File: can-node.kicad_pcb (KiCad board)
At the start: 2 copper layers, 68.6 x 66.8 mm, 36 parts, among them J1 Conn_01x02_Pin, J10 Conn_01x06_Pin, J11 Conn_01x02_Socket, J13 SDA, J14 SCL, J15 Conn_01x03_Pin, J17 Conn_01x02_Pin, J2 Conn_01x02_Pin, J3 RJ45, J4 RJ45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

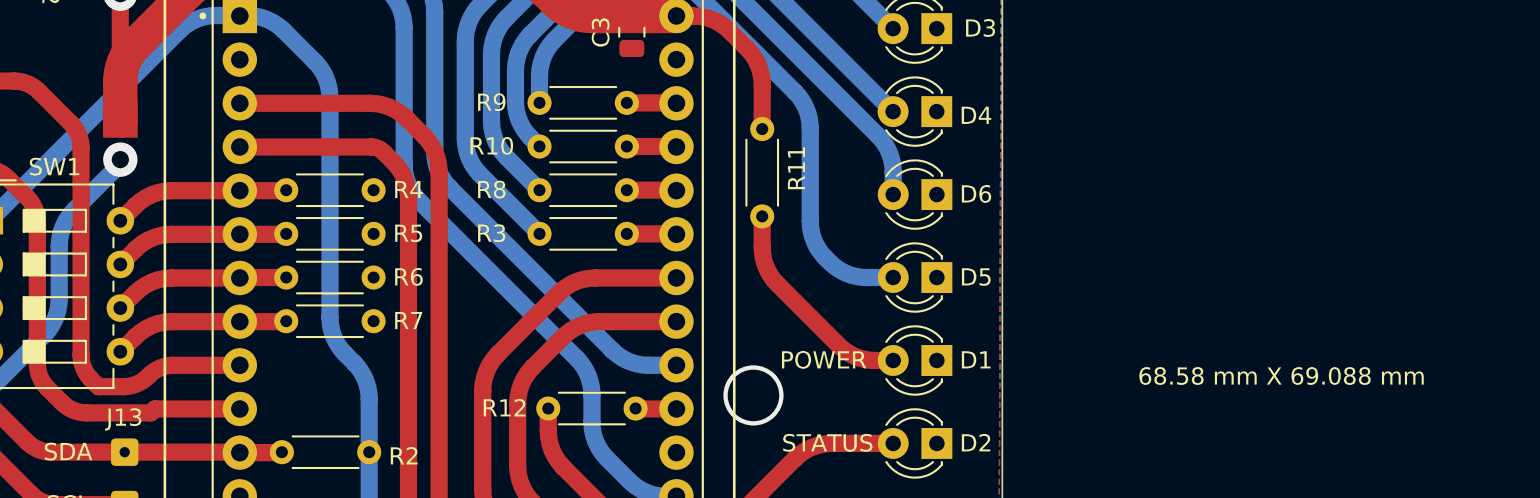
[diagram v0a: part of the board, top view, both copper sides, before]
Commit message: debug 5V trace
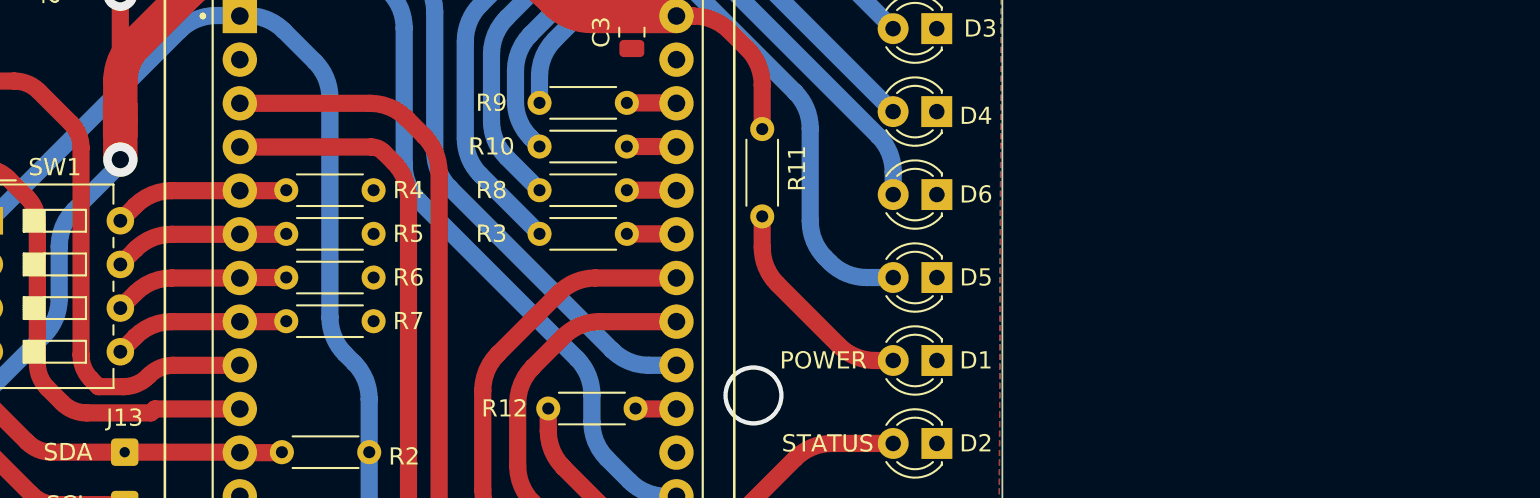
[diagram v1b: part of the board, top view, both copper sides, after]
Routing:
- net +5V: track 95.4 -> 97.7 mm
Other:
- board text removed: "68.58 mm X 69.088 mm"
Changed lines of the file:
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@@
   (gr_rect (start 102.921368 44.590812) (end 136.042369 105.651812)
     (stroke (width 0.15) (type default)) (fill none) (layer "F.CrtYd"))
-  (gr_text "68.58 mm X 69.088 mm" (at 159.512 80.772) (layer "F.SilkS")
-    (effects (font (size 1 1) (thickness 0.15)) (justify left bottom))
-  )
   (via (at 133.340815 103.061312) (size 3.5) (drill 3) (layers "F.Cu" "B.Cu") (net 0))
   (via (at 140.462 49.276) (size 3.5) (drill 3) (layers "F.Cu" "B.Cu") (net 0))
@@
   (segment (start 100.33 63.001641) (end 100.33 65.278) (width 2) (layer "F.Cu") (net 1))
   (segment (start 137.668 63.218641) (end 137.668 65.786) (width 1) (layer "F.Cu") (net 1))
+  (segment (start 100.33 67.564) (end 100.33 65.278) (width 2) (layer "F.Cu") (net 1))
   (segment (start 132.681 59.208) (end 133.657359 59.208) (width 1) (layer "F.Cu") (net 1))
   (segment (start 125.08468 57.77468) (end 125.639321 58.329321) (width 2) (layer "F.Cu") (net 1))

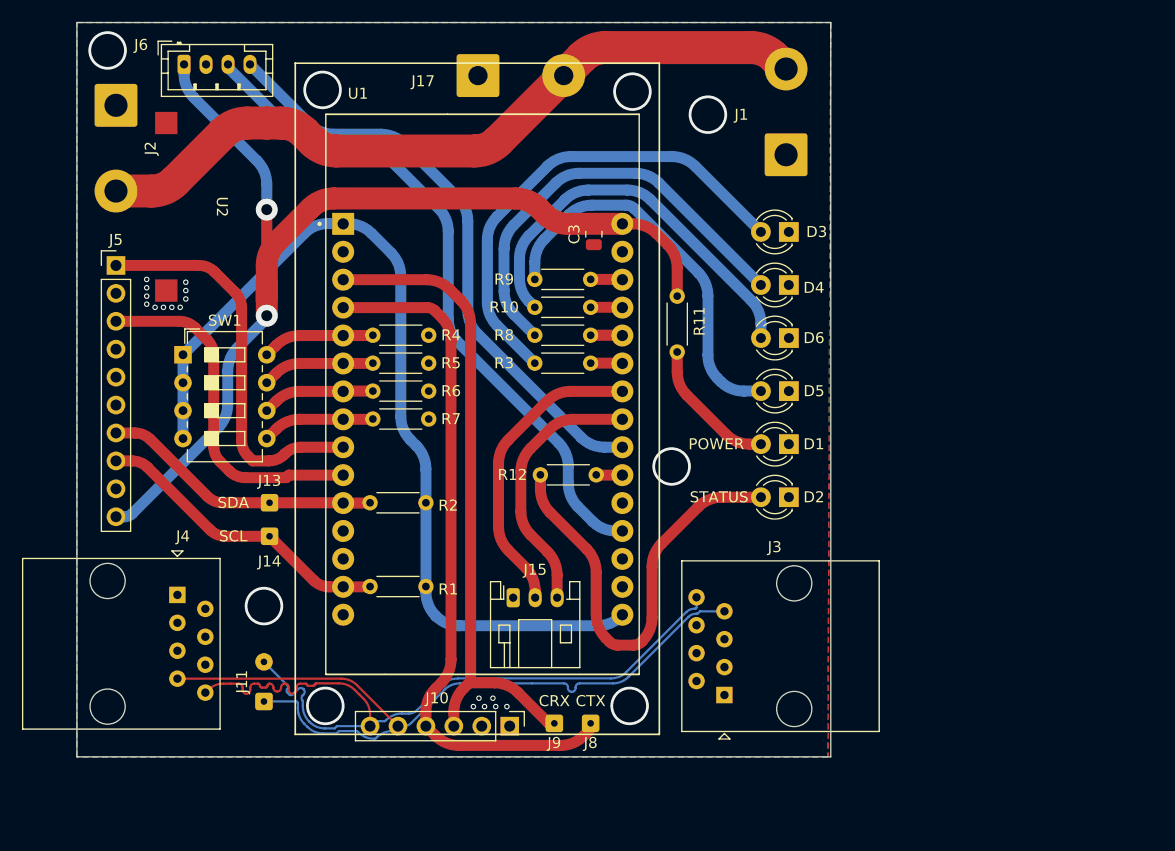
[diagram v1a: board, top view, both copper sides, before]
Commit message: add silkscreen
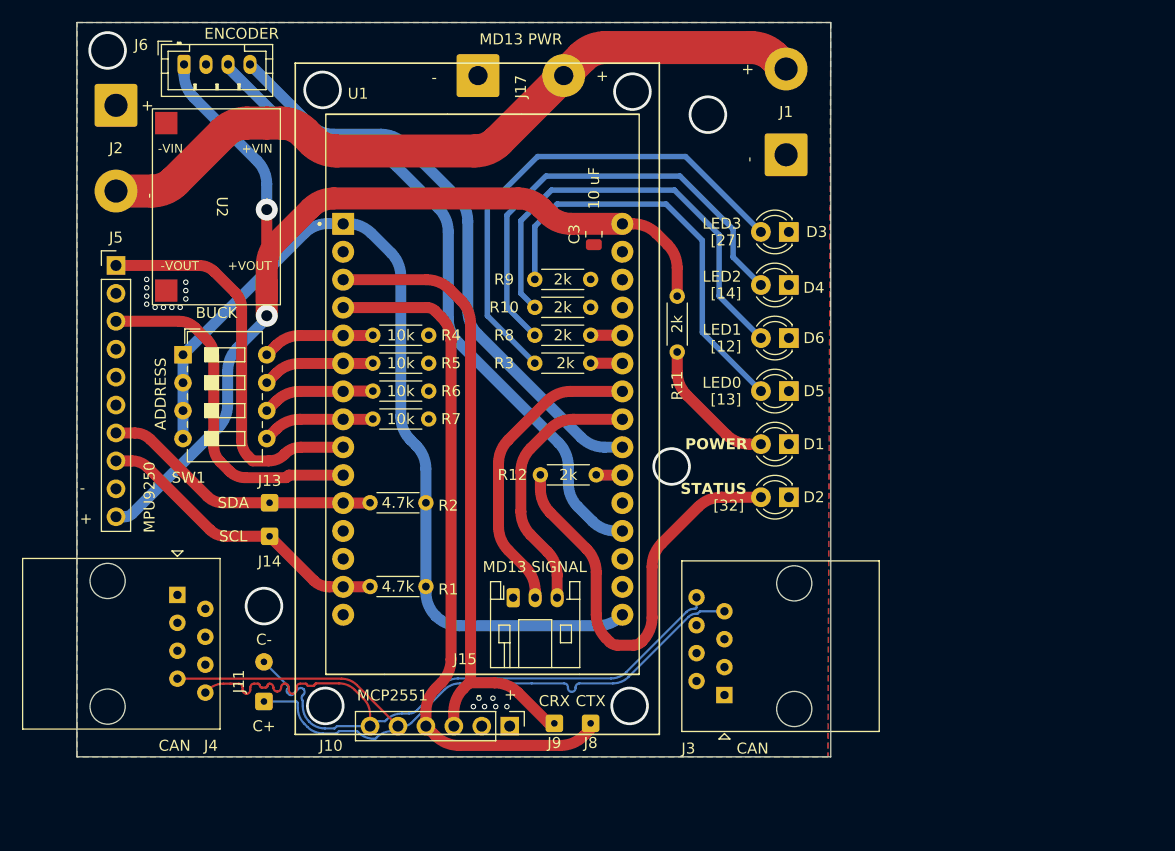
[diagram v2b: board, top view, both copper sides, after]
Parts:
- D3: value LED -> LED3
- D4: value LED -> LED2
- D5: value LED -> LED0
- D6: value LED -> LED1
- J10: value Conn_01x06_Pin -> MCP2551
- J15: value Conn_01x03_Pin -> MD13 SIGNAL
- J17: value Conn_01x02_Pin -> MD13 PWR
- J3, J4: value RJ45 -> CAN
- J5: value Conn_01x10_Pin -> MPU9250
- J6: value Conn_01x04_Pin -> ENCODER
- SW1: value SW_DIP_x04 -> ADDRESS
- U2: value ~ -> BUCK
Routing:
- net Net-(D6-A): track 36.6 -> 40.3 mm
- net LED1: track 2.90 -> 0.00 mm
- net LED0: track 2.90 -> 0.00 mm
- net Net-(D4-A): track 39.6 -> 42.2 mm
- net Net-(D5-A): track 35.9 -> 38.2 mm
- net Net-(D3-A): track 44.0 -> 45.6 mm
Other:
- board text added: "+"
- board text added: "+VIN"
- board text added: "+VOUT"
- board text added: "-"
- board text added: "-VIN"
- board text added: "-VOUT"
- board text added: "C+"
- board text added: "C-"
- board text added: "[12]"
- board text added: "[13]"
- board text added: "[14]"
- board text added: "[27]"
- board text added: "[32]"

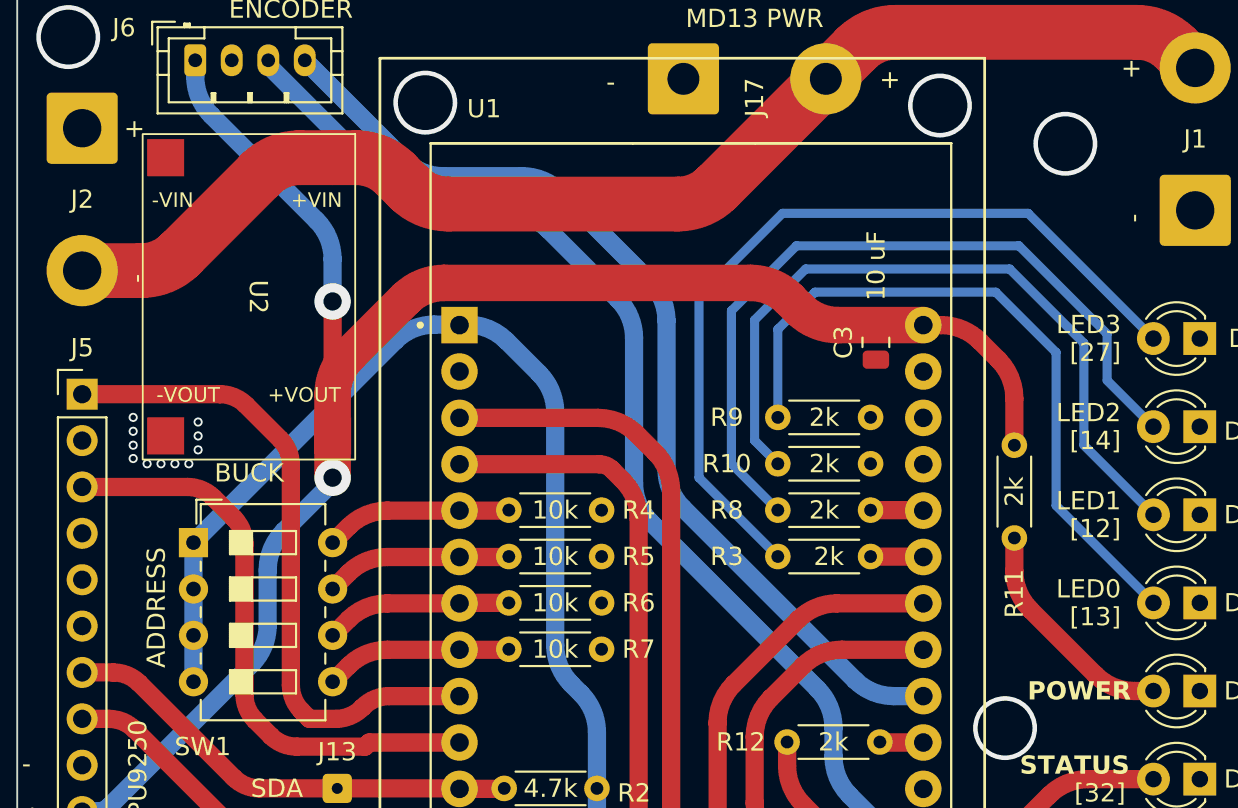
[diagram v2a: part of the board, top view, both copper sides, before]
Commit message: add CAN Rx & CAN Tx LEDs
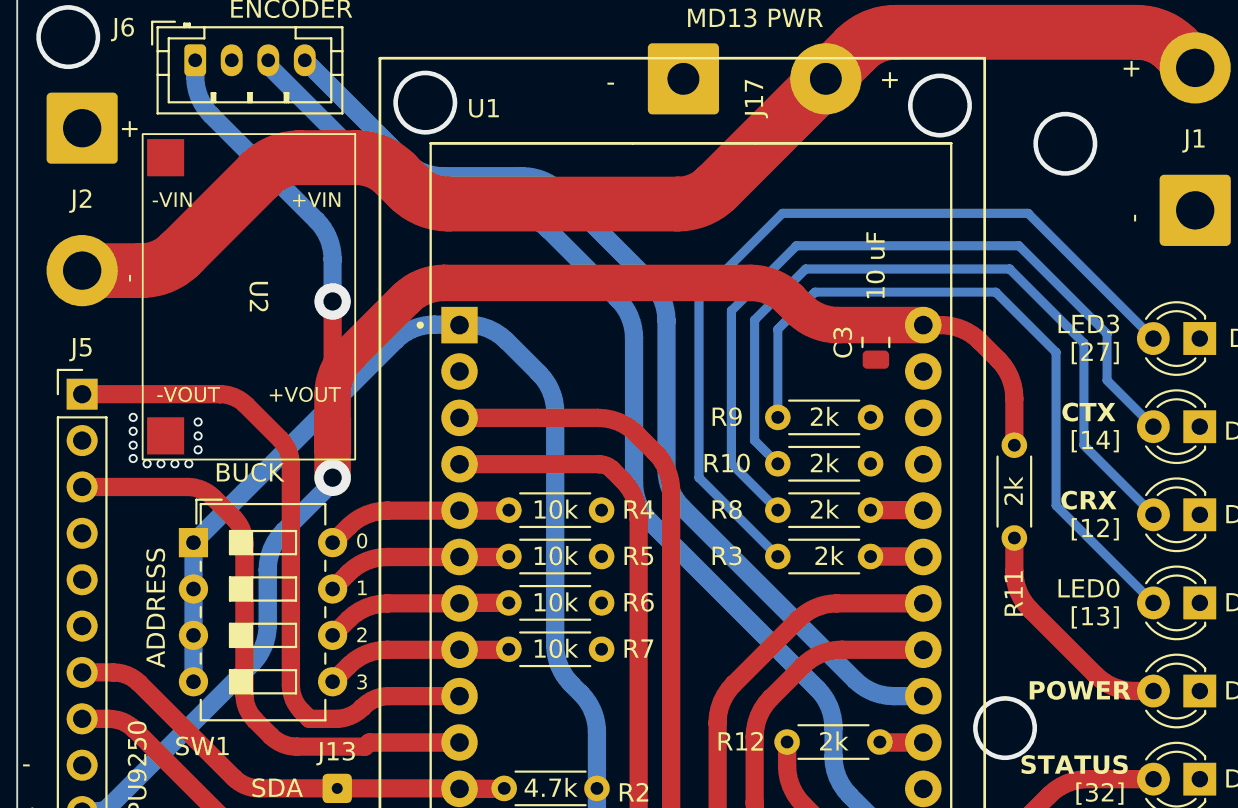
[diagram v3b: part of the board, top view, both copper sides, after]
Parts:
- D4: value LED2 -> CTX
- D6: value LED1 -> CRX
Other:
- board text added: "0 1 2 3"
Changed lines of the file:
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@@
         (effects (font (size 1 1) (thickness 0.15)))
     )
-    (fp_text value "LED1" (at 6.096 0.762) (layer "F.SilkS")
-        (effects (font (size 1 1) (thickness 0.15)))
+    (fp_text value "CRX" (at 6.096 0.762) (layer "F.SilkS" knockout)
+        (effects (font (size 1 1) (thickness 0.2) bold))
     )
     (fp_line (start -0.29 -1.236) (end -0.29 -1.08)
@@
       (rotate (xyz 0 0 0))
     )
+    (model "D:/anujv/Documents/KiCad/7.0/3dmodels/RJ45_SS_6488_FLS_Stewart.step"
+      (offset (xyz 4.5 -6.5 0))
+      (scale (xyz 1 1 1))
+      (rotate (xyz 0 0 0))
+    )
   )
   (footprint "Resistor_THT:R_Axial_DIN0204_L3.6mm_D1.6mm_P5.08mm_Horizontal" (layer "F.Cu")
@@
         (effects (font (size 1 1) (thickness 0.15)))
     )
-    (fp_text value "LED2" (at 6.091 0.762) (layer "F.SilkS")
-        (effects (font (size 1 1) (thickness 0.15)))
+    (fp_text value "CTX" (at 6.091 0.762) (layer "F.SilkS" knockout)
+        (effects (font (size 1 1) (thickness 0.2) bold))
     )
     (fp_line (start -0.29 -1.236) (end -0.29 -1.08)
@@
         (effects (font (size 1 1) (thickness 0.15)))
     )
-    (fp_text value "CAN" (at 13.716 0.254 -180) (layer "F.SilkS")
+    (fp_text value "CAN" (at 13.716 0.254) (layer "F.SilkS")
         (effects (font (size 1 1) (thickness 0.15)))
     )
@@
       (rotate (xyz 0 0 0))
     )
+    (model "D:/anujv/Documents/KiCad/7.0/3dmodels/RJ45_SS_6488_FLS_Stewart.step"
+      (offset (xyz 4.5 -6.5 0))
+      (scale (xyz 1 1 1))
+      (rotate (xyz 0 0 0))
+    )
   )
   (footprint "Connector_JST:JST_PH_S3B-PH-K_1x03_P2.00mm_Horizontal" (layer "F.Cu")
@@
     (effects (font (size 1 1) (thickness 0.15)) (justify left bottom))
   )
+  (gr_text "0\n\n1\n\n2\n\n3" (at 101.6 79.248) (layer "F.SilkS")
+    (effects (font (size 0.8 0.8) (thickness 0.15)) (justify left bottom))
+  )
   (gr_text "C-" (at 100.076 97.028) (layer "F.SilkS")
     (effects (font (size 1 1) (thickness 0.15)))
@@
     (effects (font (size 1 1) (thickness 0.15)) (justify left bottom))
   )
-  (gr_text "-" (at 90.17 56.896 90) (layer "F.SilkS")
+  (gr_text "-" (at 89.733741 56.884211 90) (layer "F.SilkS")
     (effects (font (size 1 1) (thickness 0.15)) (justify left bottom))
   )
@@
     (effects (font (size 1 1) (thickness 0.15)) (justify right))
   )
-  (gr_text "+" (at 88.9 49.022) (layer "F.SilkS")
+  (gr_text "+" (at 88.646 49.022) (layer "F.SilkS")
     (effects (font (size 1 1) (thickness 0.15)) (justify left bottom))
   )
@@
     (connect_pads yes (clearance 0.5))
     (min_thickness 1) (filled_areas_thickness no)
-    (fill (thermal_gap 1) (thermal_bridge_width 1) (smoothing fillet) (radius 3))
+    (fill yes (thermal_gap 1) (thermal_bridge_width 1) (smoothing fillet) (radius 3))
     (polygon
       (pts

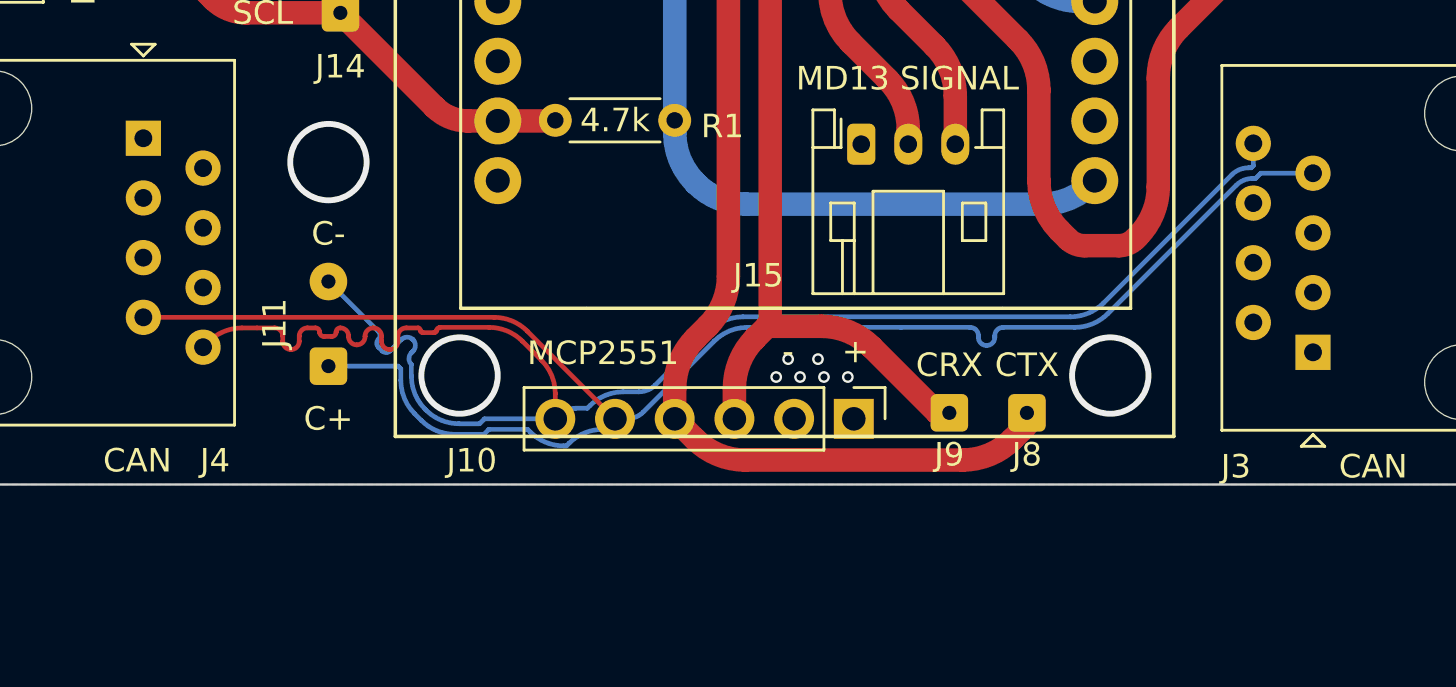
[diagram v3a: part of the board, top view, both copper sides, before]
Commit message: delete traces and move jumpers
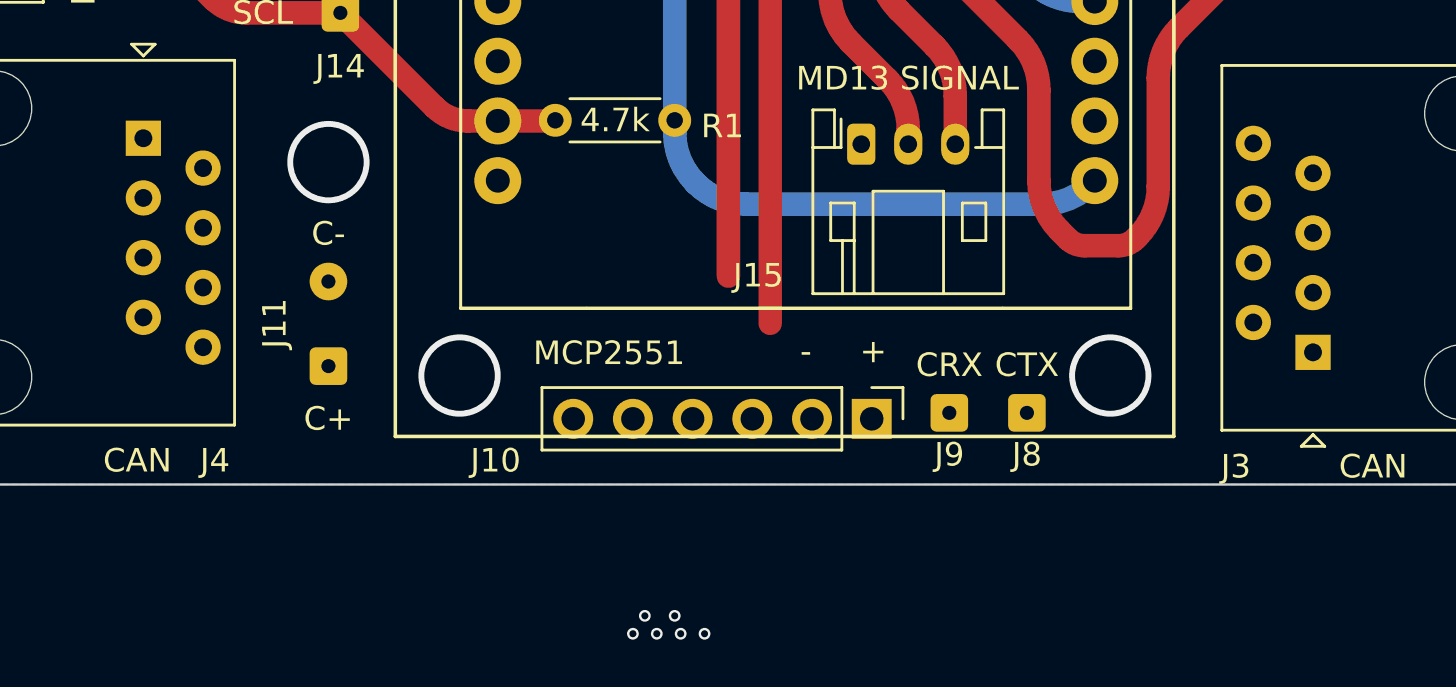
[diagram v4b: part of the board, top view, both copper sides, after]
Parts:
- moved J10 0.76 mm to (123.2, 104.9)
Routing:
- net CAN+: track 71.0 -> 0.00 mm
- net CAN-: track 70.7 -> 0.00 mm
- net CAN-Rx: track 63.4 -> 40.6 mm
- net CAN-Tx: track 59.9 -> 46.2 mm

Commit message: finish reroute
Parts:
- D3: value LED3 -> IMU CALI
- D5: value LED0 -> SYNC
- J17: value MD13 PWR -> MD13S PWR
- J8: value CTX -> CRX
- J9: value CRX -> CTX
- U2: value BUCK -> ~
- moved J6 6.13 mm to (98.8, 46.0), turned to 180 degrees
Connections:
- J6 pad 1: +5V -> ENC-B
- J6 pad 2: GND -> ENC-A
- J6 pad 3: ENC-A -> GND
- J6 pad 4: ENC-B -> +5V
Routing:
- net CAN+: track 0.00 -> 71.6 mm
- net CAN-: track 0.00 -> 71.4 mm
- net CAN-Rx: track 40.6 -> 62.7 mm
- net CAN-Tx: track 46.2 -> 59.5 mm
- net ENC-A: track 61.4 -> 63.0 mm
- net ENC-B: track 53.8 -> 55.1 mm
- net +5V: track 97.7 -> 96.4 mm
